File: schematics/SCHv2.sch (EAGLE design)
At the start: 10 parts, among them J2 POWER_JACKSLT, Q3 TIP31C

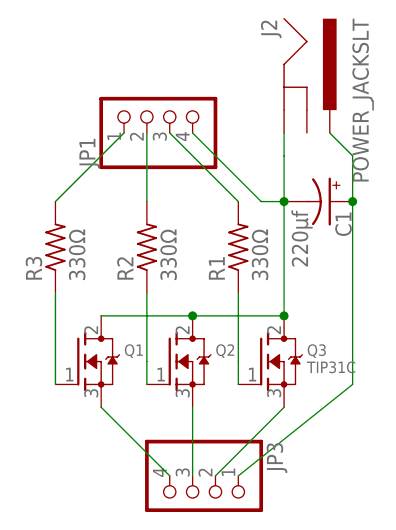
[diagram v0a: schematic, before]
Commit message: fixing wiring (power jack)
turns out the ground of the power jack was swapped with the signal pin on the jack, all fixed in this push. sadly I have 10 boards with this issue, easy fix though. 👍
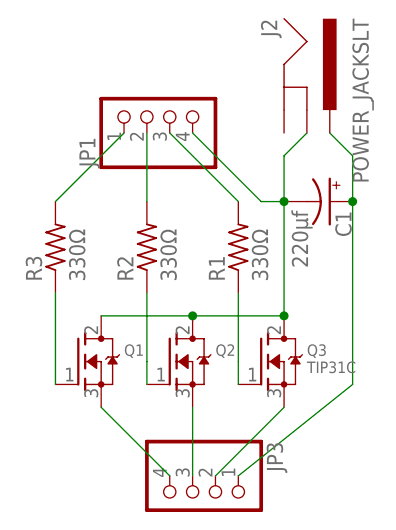
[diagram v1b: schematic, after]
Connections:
- net N$4: now also J2.GNDBREAK; no longer J2.GND
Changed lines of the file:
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@@
 <pinref part="JP1" gate="A" pin="4"/>
 <wire x1="50.8" y1="60.96" x2="50.8" y2="66.04" width="0.1524" layer="91"/>
-<pinref part="J2" gate="G$1" pin="GND"/>
-<wire x1="50.8" y1="66.04" x2="50.8" y2="68.58" width="0.1524" layer="91"/>
+<pinref part="J2" gate="G$1" pin="GNDBREAK"/>
+<wire x1="50.8" y1="66.04" x2="53.34" y2="68.58" width="0.1524" layer="91"/>
 </segment>
 </net>
